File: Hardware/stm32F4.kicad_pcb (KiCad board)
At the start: 2 copper layers, 30 parts, among them J1 USB_C_Receptacle_USB2.0_16P, J2 Conn_01x04, J5 Conn_01x20, J6 Conn_01x20, SW1 Push, SW3 Push, U1 STM32F411CCU6, U2 AMS1117-3.3, U4 2SC6, Y2 8MHz

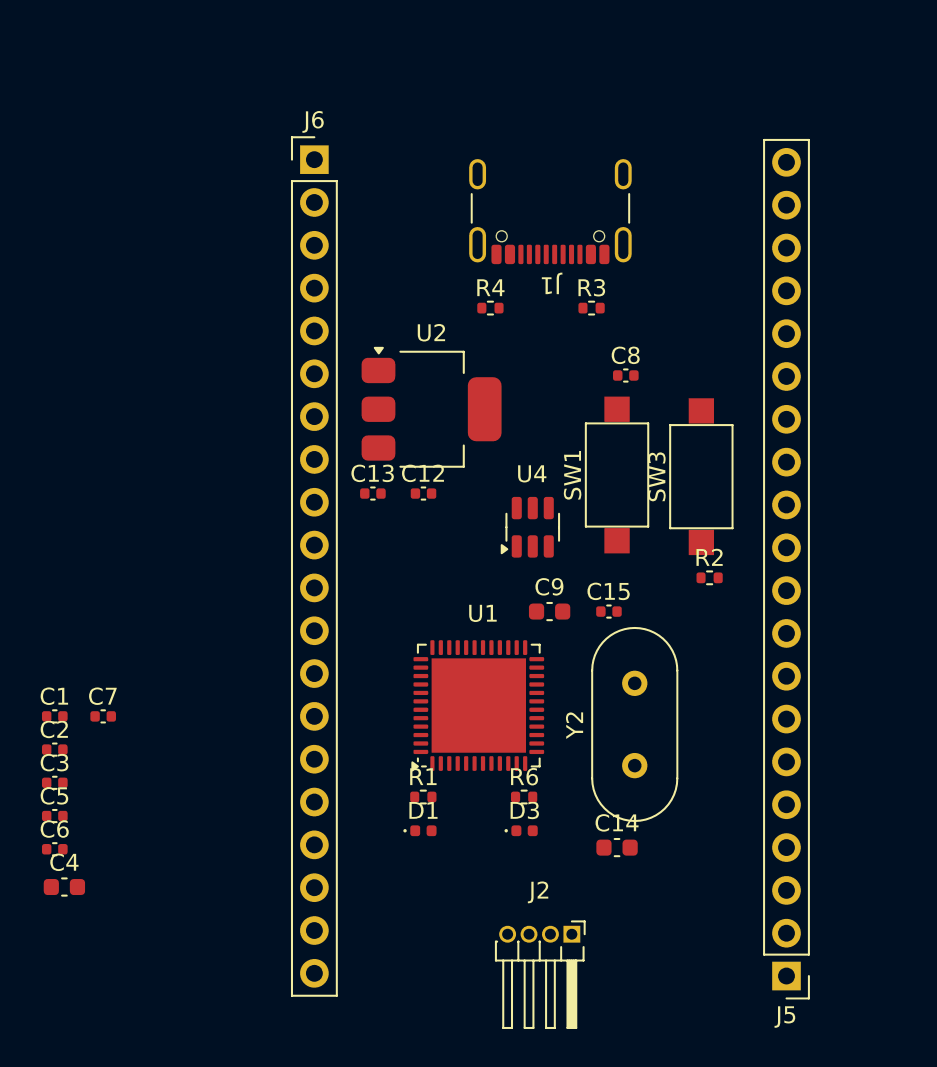
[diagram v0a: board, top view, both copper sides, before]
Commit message: PCB Layout Rough Draft and Schematic Changes
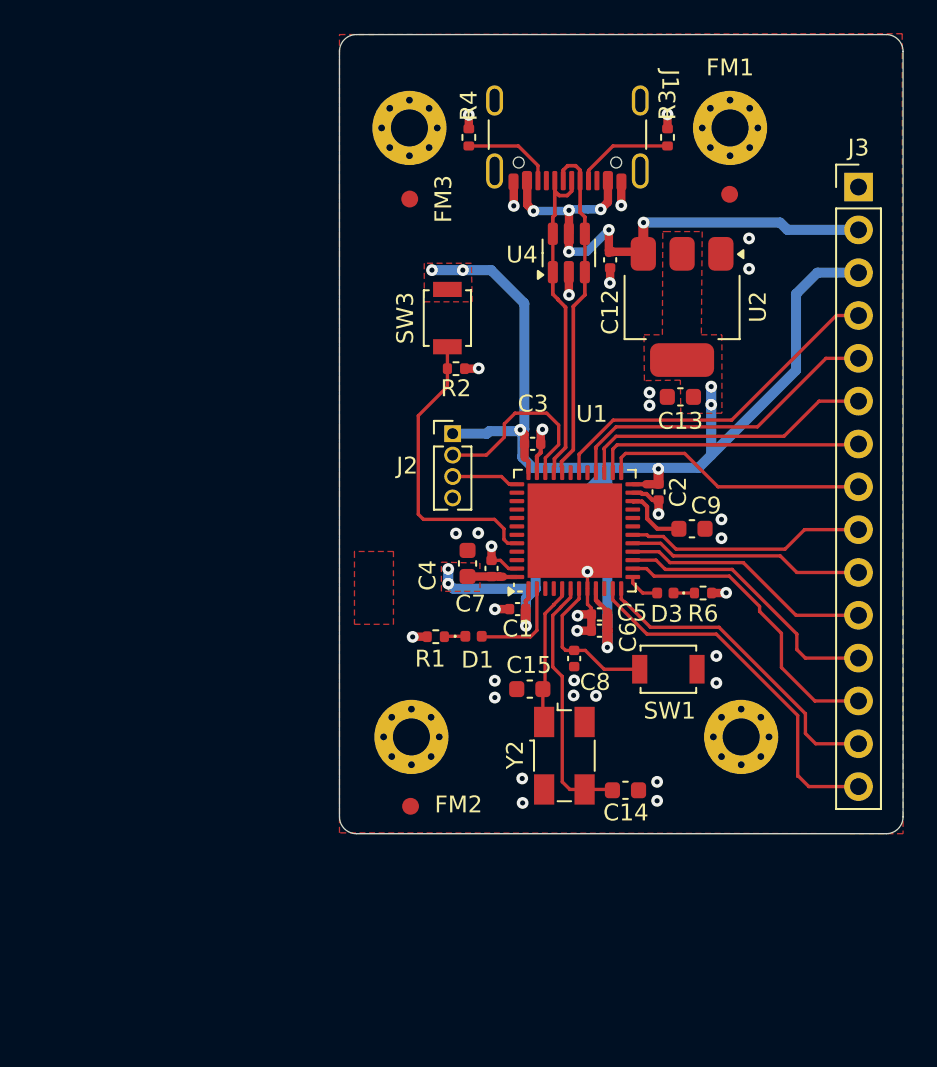
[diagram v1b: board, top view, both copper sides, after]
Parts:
- removed J5, J6: Conn_01x20, Connector_PinHeader_2.54mm:PinHeader_1x20_P2.54mm_Vertical
- added FM1: Fiducial, Fiducial:Fiducial_1mm_Mask2mm, F.Cu at (155.7, 81.2)
- added FM2: Fiducial, Fiducial:Fiducial_1mm_Mask2mm, F.Cu at (136.8, 117.4)
- added FM3: Fiducial, Fiducial:Fiducial_1mm_Mask2mm, F.Cu at (136.7, 81.4)
- added H1: MountingHole_Pad, MountingHole:MountingHole_2.2mm_M2_Pad_Via, F.Cu at (136.7, 77.2)
- added H2: MountingHole_Pad, MountingHole:MountingHole_2.2mm_M2_Pad_Via, F.Cu at (155.7, 77.2)
- added H3: MountingHole_Pad, MountingHole:MountingHole_2.2mm_M2_Pad_Via, F.Cu at (136.8, 113.3)
- added H4: MountingHole_Pad, MountingHole:MountingHole_2.2mm_M2_Pad_Via, F.Cu at (156.4, 113.3)
- added J3: Conn_01x15, Connector_PinHeader_2.54mm:PinHeader_1x15_P2.54mm_Vertical, F.Cu at (163.3, 80.7)
- C13: value 10u -> 22u; footprint Capacitor_SMD:C_0402_1005Metric -> Capacitor_SMD:C_0603_1608Metric
- C15: footprint Capacitor_SMD:C_0402_1005Metric -> Capacitor_SMD:C_0603_1608Metric
- J2: footprint Connector_PinHeader_1.27mm:PinHeader_1x04_P1.27mm_Horizontal -> Connector_PinHeader_1.27mm:PinHeader_1x04_P1.27mm_Vertical
- SW1, SW3: footprint Button_Switch_SMD:SW_SPST_CK_RS282G05A3 -> Button_Switch_SMD:SW_SPST_B3U-1000P
- U2: value AMS1117-3.3 -> AZ1117-3.3
- Y2: footprint Crystal:Crystal_HC49-4H_Vertical -> Crystal:Crystal_SMD_Abracon_ABM3B-4Pin_5.0x3.2mm
- moved C2 38.9 mm to (151.5, 98.8), turned to -90 degrees
- moved C6 34.8 mm to (148.0, 107.0), turned to 180 degrees
- moved C3 34.7 mm to (144.0, 95.9)
- moved C5 34.4 mm to (148.0, 106.1), turned to 180 degrees
- moved C4 30.7 mm to (140.1, 103.0), turned to 90 degrees
- moved J2 30.5 mm to (139.2, 95.3), turned to 0 degrees
- moved C1 28.2 mm to (143.1, 105.8), turned to 180 degrees
- moved C7 24.6 mm to (141.6, 103.3), turned to 90 degrees
- moved R2 19.5 mm to (139.4, 91.5), turned to 180 degrees
- moved C13 19.1 mm to (152.8, 93.2), turned to 180 degrees
- moved SW3 17.8 mm to (138.9, 88.5)
- moved C12 17.7 mm to (148.6, 85.0), turned to -90 degrees
- moved C8 17.1 mm to (146.5, 108.7), turned to 90 degrees
- moved U4 16.4 mm to (146.1, 84.6)
- moved D3 16.4 mm to (151.9, 104.8), turned to 180 degrees
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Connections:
- U1 pad 1: GND -> +3.3V
- U1 pad 10: /PA0 -> unconnected-(U1-PA0-Pad10)
- U1 pad 19: /PB1 -> unconnected-(U1-PB1-Pad19)
- U1 pad 20: /PB2 -> unconnected-(U1-PB2-Pad20)
- U1 pad 21: /PB10 -> unconnected-(U1-PB10-Pad21)
- U1 pad 24: GND -> +3.3V
- U1 pad 29: /PA8 -> unconnected-(U1-PA8-Pad29)
- U1 pad 3: /PC14 -> unconnected-(U1-PC14-Pad3)
- U1 pad 31: /PA10 -> unconnected-(U1-PA10-Pad31)
- U1 pad 36: GND -> +3.3V
- U1 pad 38: /PA15 -> unconnected-(U1-PA15-Pad38)
- U1 pad 39: /PB3 -> unconnected-(U1-PB3-Pad39)
- U1 pad 4: /PC15 -> unconnected-(U1-PC15-Pad4)
- U1 pad 40: /PB4 -> unconnected-(U1-PB4-Pad40)
- U1 pad 41: /PB5 -> unconnected-(U1-PB5-Pad41)
- U1 pad 42: /PB6 -> unconnected-(U1-PB6-Pad42)
- U1 pad 43: /PB7 -> unconnected-(U1-PB7-Pad43)
- U1 pad 45: /PB8 -> unconnected-(U1-PB8-Pad45)
- U1 pad 46: /PB9 -> unconnected-(U1-PB9-Pad46)
- U1 pad 48: GND -> +3.3V
- U1 pad 9: GND -> +3.3V
- U4 pad 4: unconnected-(U4-I/O2-Pad4) -> /USB_D-
- U4 pad 5: +3.3V -> +5V
- U4 pad 6: unconnected-(U4-I/O1-Pad6) -> /USB_D+
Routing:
- net +3.3V: track 0.00 -> 94.2 mm, vias 0 -> 10
- net +5V: track 0.00 -> 31.6 mm, vias 0 -> 6
- net GND: track 0.00 -> 26.1 mm, vias 0 -> 35
- net /PA1: track 0.00 -> 21.9 mm
- net /PA9: track 0.00 -> 21.1 mm
- net /USB_D+: track 0.00 -> 20.6 mm
- net /USB_D-: track 0.00 -> 20.5 mm
- net /PB15: track 0.00 -> 19.3 mm
- net /PA2: track 0.00 -> 18.9 mm
- net /PA4: track 0.00 -> 18.0 mm
- net /PB14: track 0.00 -> 17.7 mm
- net /BOOT0: track 0.00 -> 17.6 mm
- net /PA5: track 0.00 -> 16.3 mm
- net /PB13: track 0.00 -> 16.1 mm
- net /PB12: track 0.00 -> 15.9 mm
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- added copper zone on F.Cu, net +3.3V
- added copper zone on F.Cu, net GND
- added copper zone on In1.Cu, net GND
- added copper zone on In2.Cu, net GND
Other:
- board outline added: 33.4 x 47.4 mm
- copper layers 2 -> 4
